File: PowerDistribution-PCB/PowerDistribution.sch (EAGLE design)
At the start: 47 parts, among them IC1 MAX3041CUE, IC2 MAX3041CUE, IC3 MAX3041CUE, IC4 MAX3041CUE, IC9 SN75176ASOIC

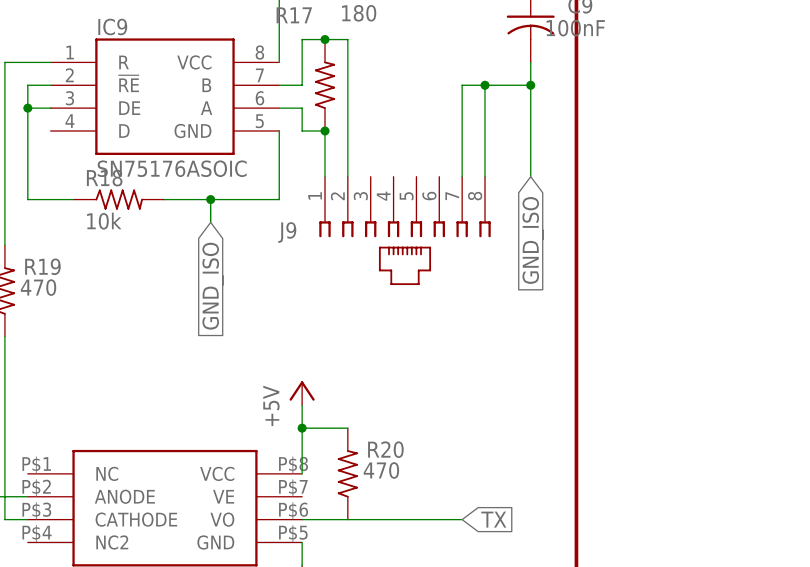
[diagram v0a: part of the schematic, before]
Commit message: Finish routing power distribution PCB; still need to fit to case
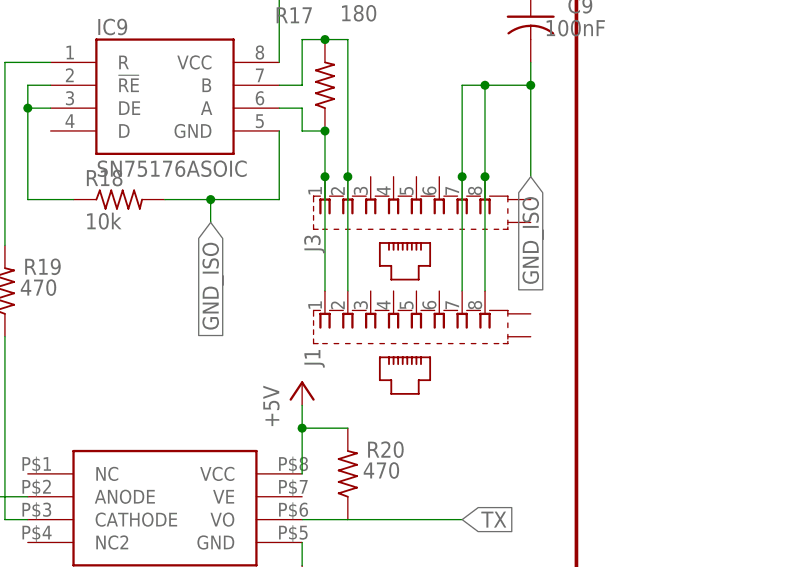
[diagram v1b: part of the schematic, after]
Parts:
- removed J9: (no value), con-amp:520426-4
- added J1, J3: (no value), con-amp:555153-1
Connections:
- new net N$35: J1.3
- new net N$36: J1.4
- new net N$37: J1.5
- new net N$38: J1.6
- net GND_ISO: now also J1.7, J1.8, J3.7, J3.8; no longer J9.7, J9.8
- net RS485A9: now also J1.1, J3.1; no longer J9.1
- net RS485B9: now also J1.2, J3.2; no longer J9.2
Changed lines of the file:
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@@
 <part name="R18" library="adafruit" deviceset="R-US_" device="R0603" value="10k"/>
 <part name="C9" library="adafruit" deviceset="C-US" device="C0603" value="100nF"/>
-<part name="J9" library="con-amp" deviceset="520426-4" device=""/>
 <part name="R19" library="adafruit" deviceset="R-US_" device="R0603" value="470"/>
 <part name="R20" library="adafruit" deviceset="R-US_" device="R0603" value="470"/>
@@
 <part name="R15" library="adafruit" deviceset="R-US_" device="R0603" value="180"/>
 <part name="R16" library="adafruit" deviceset="R-US_" device="R0603" value="180"/>
+<part name="J3" library="con-amp" deviceset="555153-1" device=""/>
+<part name="J1" library="con-amp" deviceset="555153-1" device=""/>
 </parts>
 <sheets>
@@
 <attribute name="VALUE" x="197.104" y="94.361" size="1.778" layer="96"/>
 </instance>
-<instance part="J9" gate="G$1" x="180.34" y="73.66" smashed="yes" rot="MR270">
-<attribute name="NAME" x="167.64" y="73.66" size="1.778" layer="95" rot="MR180"/>
-<attribute name="VALUE" x="193.548" y="78.74" size="1.778" layer="96" rot="MR270"/>
-</instance>
 <instance part="R19" gate="G$1" x="137.16" y="66.04" smashed="yes" rot="R90">
 <attribute name="NAME" x="143.51" y="69.6214" size="1.778" layer="95" rot="R180"/>
@@
 <attribute name="VALUE" x="252.222" y="-148.59" size="1.778" layer="96" rot="R180"/>
 </instance>
+<instance part="J3" gate="G$1" x="182.88" y="76.2" rot="MR270"/>
+<instance part="J1" gate="G$1" x="182.88" y="63.5" rot="MR270"/>
 </instances>
 <busses>
@@
 <pinref part="R17" gate="G$1" pin="2"/>
 <pinref part="IC9" gate="G$1" pin="B"/>
-<pinref part="J9" gate="G$1" pin="2"/>
 <wire x1="172.72" y1="93.98" x2="175.26" y2="93.98" width="0.1524" layer="91"/>
 <wire x1="175.26" y1="93.98" x2="175.26" y2="78.74" width="0.1524" layer="91"/>
 <junction x="172.72" y="93.98"/>
+<pinref part="J3" gate="G$1" pin="2"/>
+<pinref part="J1" gate="G$1" pin="2"/>
+<junction x="175.26" y="78.74"/>
+<wire x1="175.26" y1="78.74" x2="175.26" y2="66.04" width="0.1524" layer="91"/>
 </segment>
 </net>
@@
 <pinref part="IC9" gate="G$1" pin="A"/>
 <pinref part="R17" gate="G$1" pin="1"/>
-<pinref part="J9" gate="G$1" pin="1"/>
 <wire x1="172.72" y1="83.82" x2="172.72" y2="78.74" width="0.1524" layer="91"/>
 <junction x="172.72" y="83.82"/>
+<pinref part="J3" gate="G$1" pin="1"/>
+<pinref part="J1" gate="G$1" pin="1"/>
+<junction x="172.72" y="78.74"/>
+<wire x1="172.72" y1="78.74" x2="172.72" y2="66.04" width="0.1524" layer="91"/>
 </segment>
 </net>
@@
 <label x="195.58" y="78.74" size="1.778" layer="95" rot="R270" xref="yes"/>
 <wire x1="195.58" y1="88.9" x2="195.58" y2="78.74" width="0.1524" layer="91"/>
-<pinref part="J9" gate="G$1" pin="8"/>
 <wire x1="190.5" y1="78.74" x2="190.5" y2="88.9" width="0.1524" layer="91"/>
 <wire x1="190.5" y1="88.9" x2="187.96" y2="88.9" width="0.1524" layer="91"/>
-<pinref part="J9" gate="G$1" pin="7"/>
 <wire x1="187.96" y1="88.9" x2="187.96" y2="78.74" width="0.1524" layer="91"/>
 <junction x="190.5" y="88.9"/>
@@
 <wire x1="195.58" y1="91.44" x2="195.58" y2="88.9" width="0.1524" layer="91"/>
 <junction x="195.58" y="88.9"/>
+<pinref part="J3" gate="G$1" pin="7"/>
+<pinref part="J3" gate="G$1" pin="8"/>
+<pinref part="J1" gate="G$1" pin="7"/>
+<pinref part="J1" gate="G$1" pin="8"/>
+<junction x="190.5" y="78.74"/>
+<junction x="187.96" y="78.74"/>
+<wire x1="190.5" y1="78.74" x2="190.5" y2="66.04" width="0.1524" layer="91"/>
+<wire x1="187.96" y1="78.74" x2="187.96" y2="66.04" width="0.1524" layer="91"/>
 </segment>
 <segment>
@@
 </segment>
 </net>
+<net name="N$35" class="0">
+<segment>
+<pinref part="J1" gate="G$1" pin="3"/>
+<pinref part="J1" gate="G$1" pin="3"/>
+</segment>
+</net>
+<net name="N$36" class="0">
+<segment>
+<pinref part="J1" gate="G$1" pin="4"/>
+<pinref part="J1" gate="G$1" pin="4"/>
+</segment>
+</net>
+<net name="N$37" class="0">
+<segment>
+<pinref part="J1" gate="G$1" pin="5"/>
+<pinref part="J1" gate="G$1" pin="5"/>
+</segment>
+</net>
+<net name="N$38" class="0">
+<segment>
+<pinref part="J1" gate="G$1" pin="6"/>
+<pinref part="J1" gate="G$1" pin="6"/>
+</segment>
+</net>

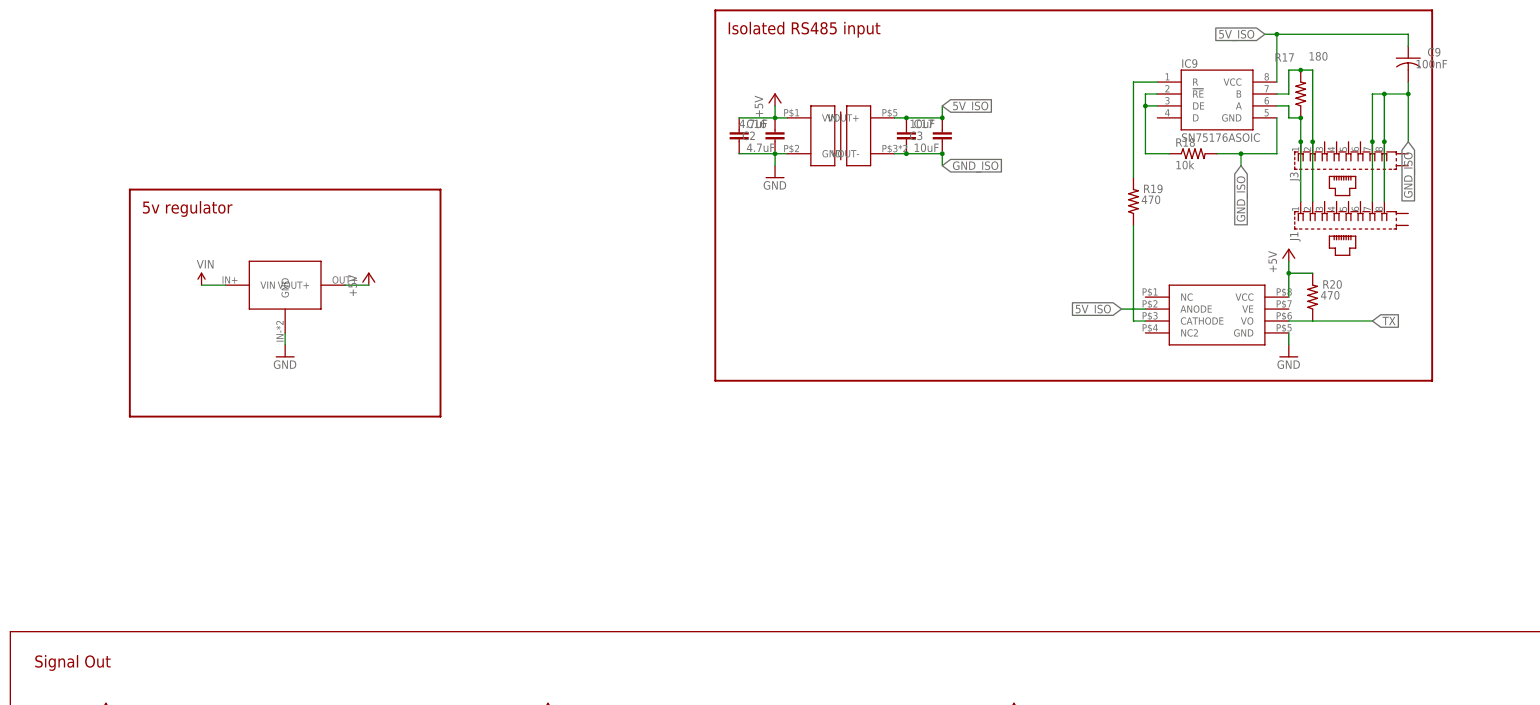
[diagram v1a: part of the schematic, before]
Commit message: Power Distribution: Finish layout, add mouting holes at edges (likely not quite enough), release RevA
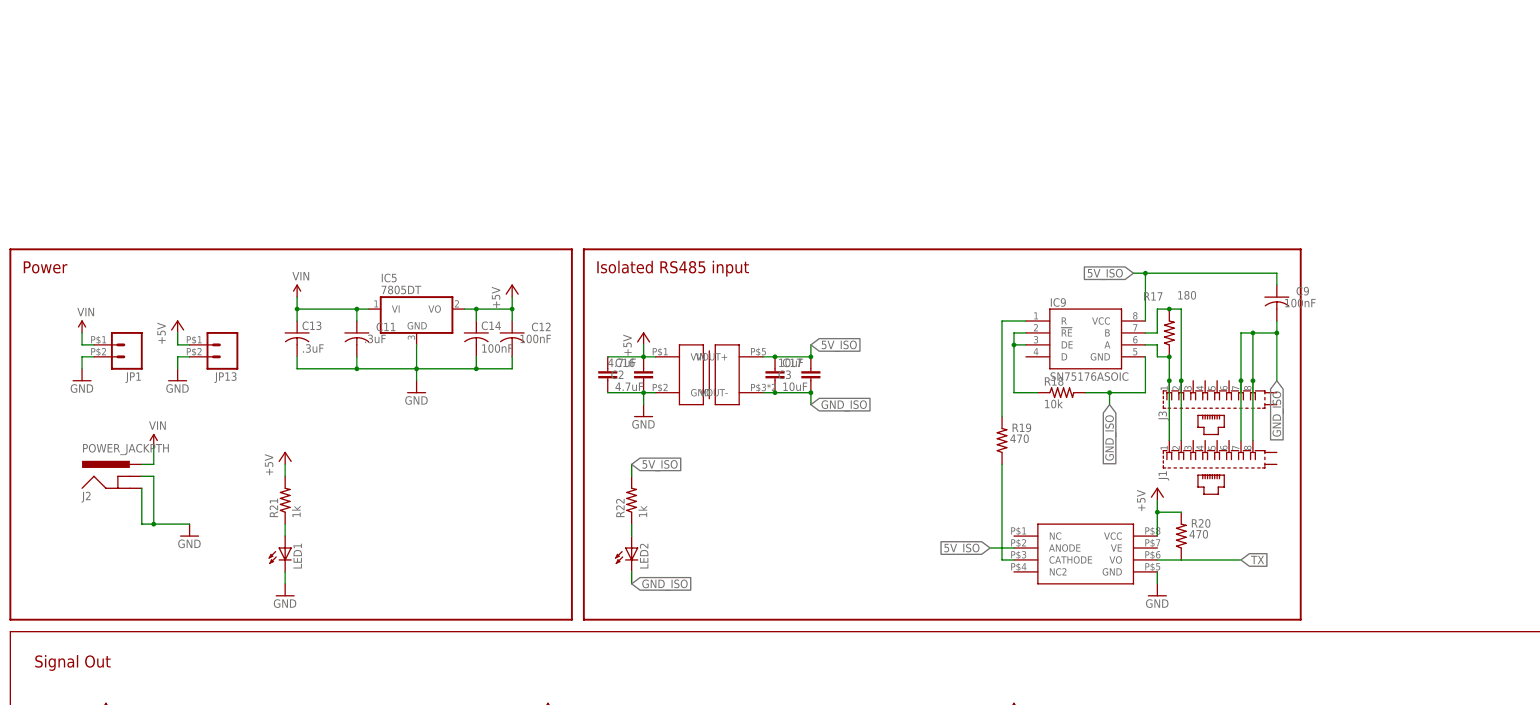
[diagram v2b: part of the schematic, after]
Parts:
- removed U$19: DC_DC, blinkinlabs:DC_DC
- added C11, C13: .3uF, adafruit:C-USC0603K
- added C12, C14: 100nF, adafruit:C-USC0603K
- added IC5: 7805DT, linear:7805DT
- added J2: POWER_JACKPTH, SparkFun:POWER_JACKPTH
- added JP1, JP13: (no value), SparkFun:M026.35MM
- added LED1, LED2: (no value), SparkFun:LED5MM
- added R21, R22: 1k, adafruit:R-US_R0603
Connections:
- new net N$39: LED1.A, R21.1
- new net N$40: LED2.A, R22.1
- net +5V: now also C12.1, C14.1, IC5.VO, JP13.1, R21.2; no longer U$19.VOUT+
- net 5V_ISO: now also R22.2
- net GND: now also C11.2, C12.2, C13.2, C14.2, IC5.GND, J2.GND, J2.GNDBREAK, JP1.2, JP13.2, LED1.C; no longer U$19.GND
- net GND_ISO: now also LED2.C
- net VIN: now also C11.1, C13.1, IC5.VI, J2.PWR, JP1.1; no longer U$19.VIN
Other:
- note added: "Power"
- note removed: "5v regulator"
- moved on the sheet: C16, C17, C2, C3, C9, IC9, J1, J3, R17, R18, R19, R20
